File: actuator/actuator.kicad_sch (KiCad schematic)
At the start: 18 parts, among them J1 Conn_01x12, J2 Conn_01x40_Socket

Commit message: move piezo smd connector, rework pads & adhesive
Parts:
- TP2: footprint TestPoint:TestPoint_THTPad_1.0x1.0mm_Drill0.5mm -> TestPoint:TestPoint_THTPad_D1.0mm_Drill0.5mm
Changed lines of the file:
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@@
       (effects (font (size 1.27 1.27)) hide)
     )
-    (property "Footprint" "TestPoint:TestPoint_THTPad_1.0x1.0mm_Drill0.5mm" (at 88.9 135.89 0)
+    (property "Footprint" "TestPoint:TestPoint_THTPad_D1.0mm_Drill0.5mm" (at 88.9 135.89 0)
       (effects (font (size 1.27 1.27)) hide)
     )

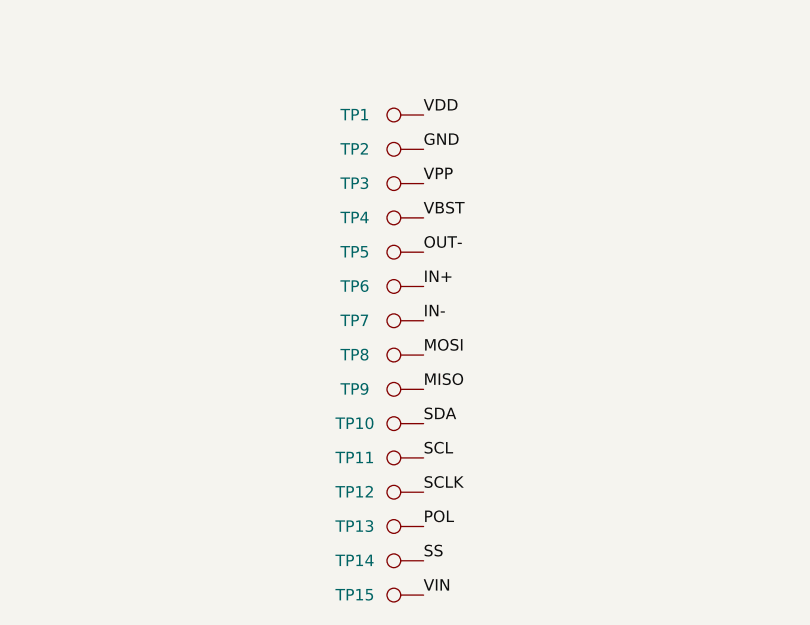
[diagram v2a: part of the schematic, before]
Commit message: actuator move testpoints to subsheets
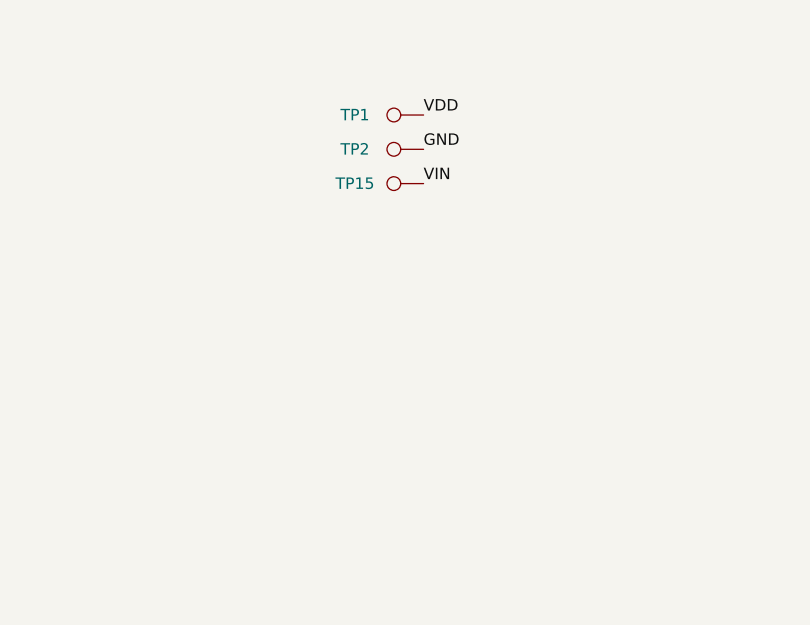
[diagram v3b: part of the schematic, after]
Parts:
- removed TP10, TP11, TP12, TP13, TP14, TP3, TP4, TP5, TP6, TP7, TP8, TP9: TestPoint, TestPoint:TestPoint_THTPad_D1.0mm_Drill0.5mm, symbol Connector:TestPoint
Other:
- moved on the sheet: TP15
